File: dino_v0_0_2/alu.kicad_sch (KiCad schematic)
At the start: 0 parts

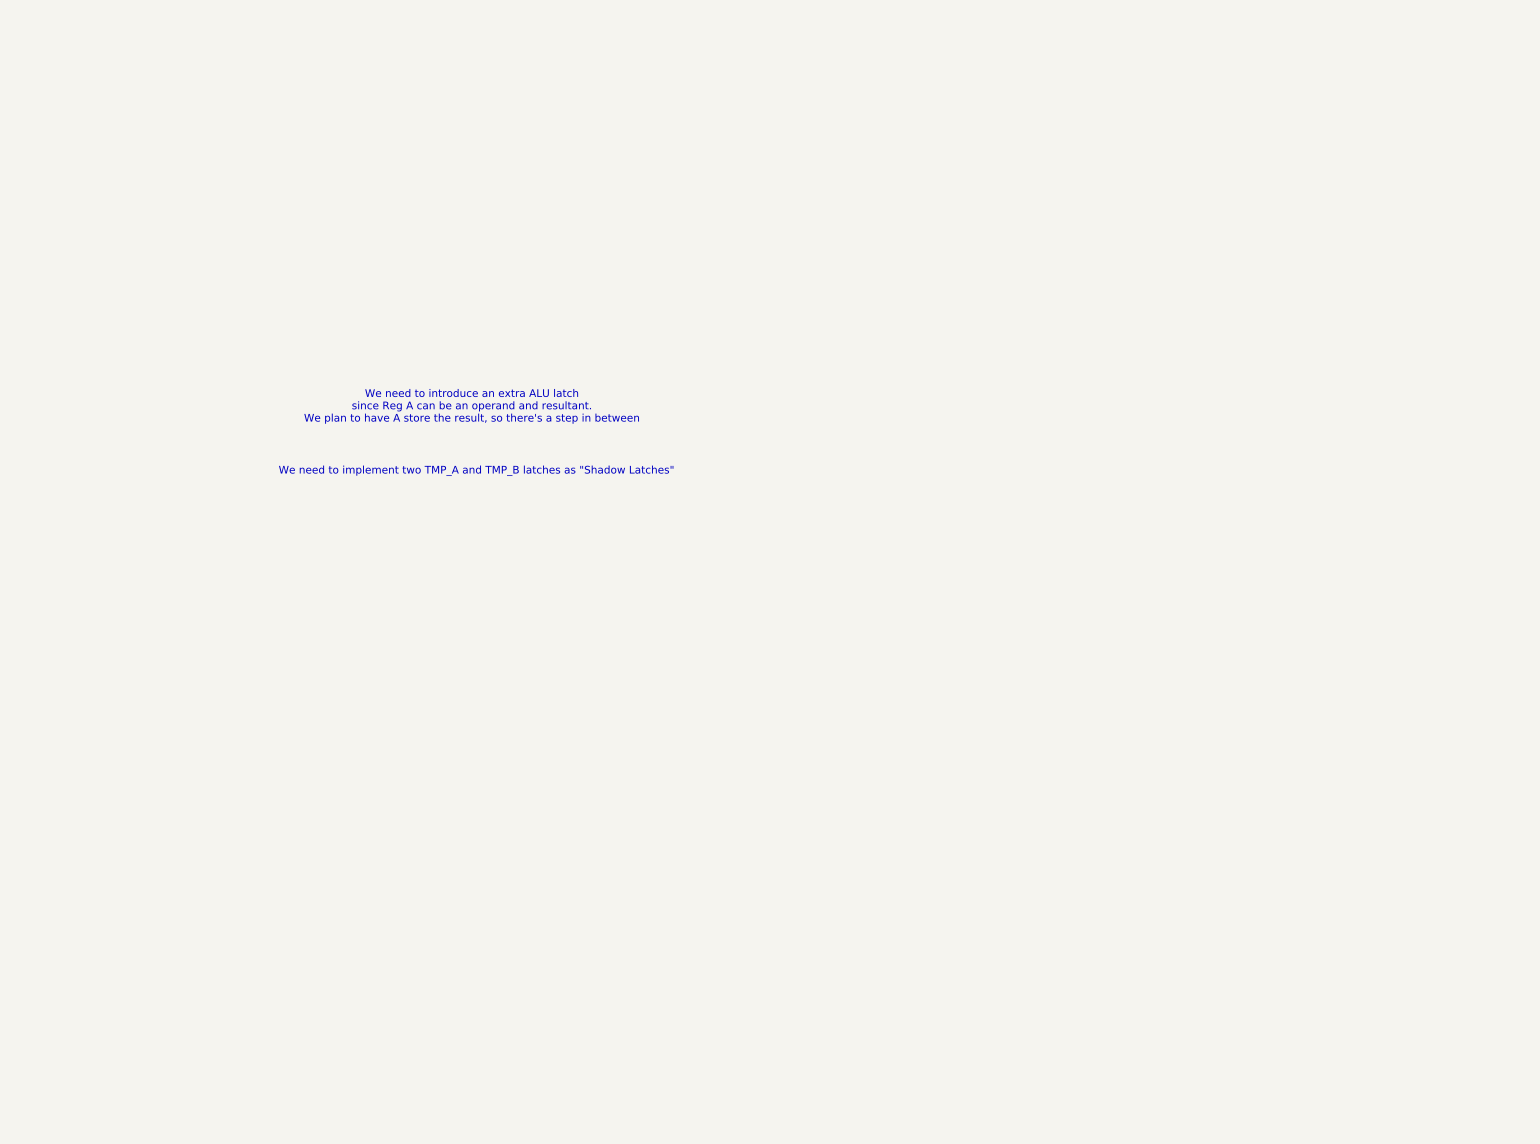
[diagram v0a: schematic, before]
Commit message: DINO v0.0.3: complete ALU/control-word, add MAR+reset sheets, wire reset circuit
ALU sheet: flags register moved from '173 (not in stock) to '273 + a '157
mux to emulate the missing load-enable pins; Z-detect built from a NOR+AND
De Morgan tree instead of a '260; ALU_CIN built from NAND(SA1,SA0) reusing
two already-placed spare gates instead of a dedicated XOR/'86. Sheet is
now fully wired and netlist-clean.

Control word sheet: all 16 CW bits assigned and wired (3x '138 decoders
for the load/source/misc fields, direct bus taps for HALT/PC_MAR_MUX/
PC_UP/END and the ALU SA[2:0] select). Found and fixed several cross-
sheet signal-name mismatches this uncovered (OUT_REG_LOAD/REG_OUT_LOAD,
PC_MAR_MUX/PC_MUX, T-state counter labels, a mirror-reversed IRB->ROM-
address buffer in microcode).

New: MAR and reset sheets, wired into the root hierarchy. Reset circuit
is a from-scratch design: RC+button+74HC14 Schmitt front end feeds the
async PRESET of the clock cluster's spare '74 half (U27B), synchronizing
release to CLK; its Q/~Q fan out to the flags register, the T-state
counter's clear, and (OR'd with the existing microcode-driven PC_CLEAR,
reusing spare gates on the same '02) the PC counters' clear.

Deprecated 7 schematic files no longer referenced by the root sheet's
hierarchy into dino_v0_0_2/deprecated/. Added docs/notes/kicad_netlist.py,
a .kicad_sch connectivity auditor (pin/net resolution incl. buses and
same-name local-label merging) used throughout this session to find the
above bugs; archived completed-work docs into docs/notes/Done/ and
rewrote dino_session_state.md as the current authoritative state+TODO.

Co-Authored-By: Claude Sonnet 5 <noreply@anthropic.com>
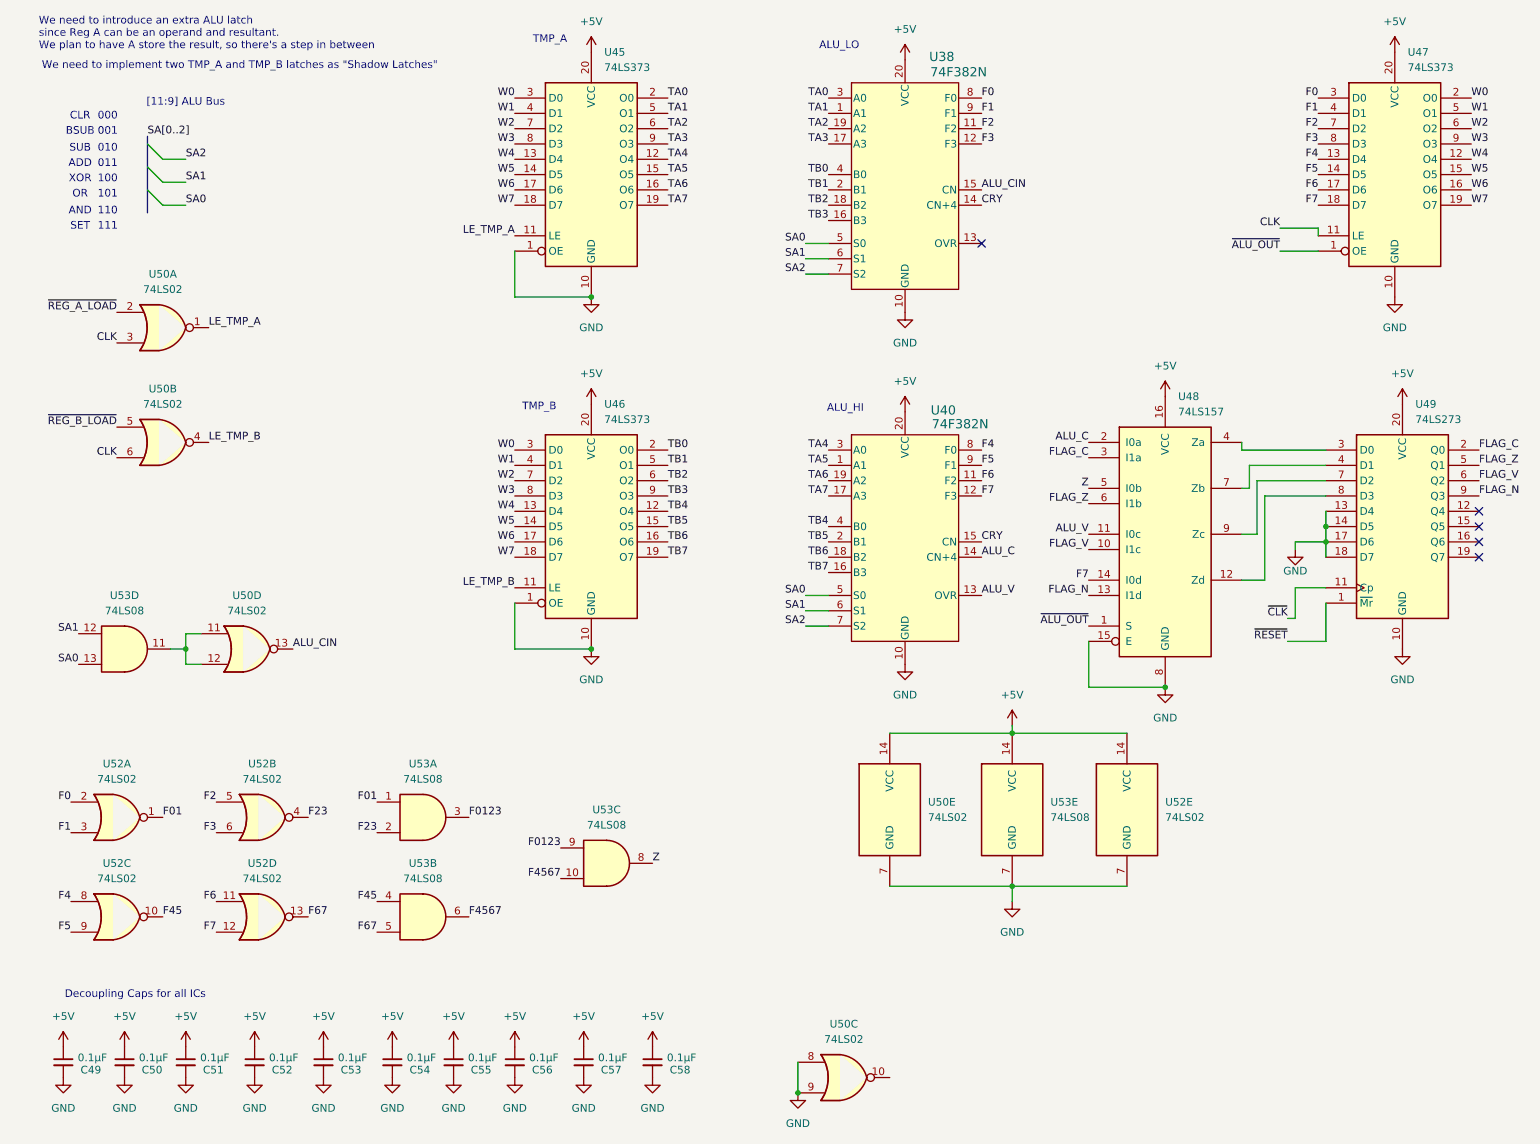
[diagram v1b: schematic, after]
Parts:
- added C49, C50, C51, C52, C53, C54, C55, C56, C57, C58: 0.1µF, symbol Device:C_Small
- added U38, U40: 74F382N, PDIP20_26P42X6P6_ONS, symbol 2026-07-13_03-50-17:74F382PC
- added U45, U46, U47: 74LS373, symbol 74xx:74LS373
- added U48: 74LS157, symbol 74xx:74LS157
- added U49: 74LS273, symbol 74xx:74LS273
- added U50, U52: 74LS02, symbol 74xx:74LS02
- added U53: 74LS08, symbol 74xx:74LS08
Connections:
- new net: U48.4 (Za), U49.3 (D0)
- new net: U48.7 (Zb), U49.4 (D1)
- new net: U48.9 (Zc), U49.7 (D2)
- new net: U48.12 (Zd), U49.8 (D3)
- new net: U50.11, U50.12, U53.11
- new net +5V: C49.1, C50.1, C51.1, C52.1, C53.1, C54.1, C55.1, C56.1, C57.1, C58.1, U38.20 (VCC), U40.20 (VCC), U45.20 (VCC), U46.20 (VCC), U47.20 (VCC), U48.16 (VCC), U49.20 (VCC), U50.14 (VCC), U52.14 (VCC), U53.14 (VCC)
- new net ALU_C: U40.14 (CN+4), U48.2 (I0a)
- new net ALU_CIN: U38.15 (CN), U50.13
- new net ALU_V: U40.13 (OVR), U48.11 (I0c)
- new net CLK: U47.11 (LE), U50.3, U50.6
- new net CRY: U38.14 (CN+4), U40.15 (CN)
- new net F0: U38.8 (F0), U47.3 (D0), U52.2
- new net F01: U52.1, U53.1
- new net F0123: U53.3, U53.9
- new net F1: U38.9 (F1), U47.4 (D1), U52.3
- new net F2: U38.11 (F2), U47.7 (D2), U52.5
- new net F23: U52.4, U53.2
- new net F3: U38.12 (F3), U47.8 (D3), U52.6
- new net F4: U40.8 (F0), U47.13 (D4), U52.8
- new net F45: U52.10, U53.4
- new net F4567: U53.10, U53.6
- new net F5: U40.9 (F1), U47.14 (D5), U52.9
- new net F6: U40.11 (F2), U47.17 (D6), U52.11
- new net F67: U52.13, U53.5
- new net F7: U40.12 (F3), U47.18 (D7), U48.14 (I0d), U52.12
- new net FLAG_C: U48.3 (I1a), U49.2 (Q0)
- new net FLAG_N: U48.13 (I1d), U49.9 (Q3)
- new net FLAG_V: U48.10 (I1c), U49.6 (Q2)
- new net FLAG_Z: U48.6 (I1b), U49.5 (Q1)
- new net GND: C49.2, C50.2, C51.2, C52.2, C53.2, C54.2, C55.2, C56.2, C57.2, C58.2, U38.10 (GND), U40.10 (GND), U45.1 (OE), U45.10 (GND), U46.1 (OE), U46.10 (GND), U47.10 (GND), U48.15 (E), U48.8 (GND), U49.10 (GND), U49.13 (D4), U49.14 (D5), U49.17 (D6), U49.18 (D7), U50.7 (GND), U50.8, U50.9, U52.7 (GND), U53.7 (GND)
- new net LE_TMP_A: U45.11 (LE), U50.1
- new net LE_TMP_B: U46.11 (LE), U50.4
- new net SA0: U38.5 (S0), U40.5 (S0), U53.13
- new net SA1: U38.6 (S1), U40.6 (S1), U53.12
- new net SA2: U38.7 (S2), U40.7 (S2)
- new net TA0: U38.3 (A0), U45.2 (O0)
- new net TA1: U38.1 (A1), U45.5 (O1)
- new net TA2: U38.19 (A2), U45.6 (O2)
- new net TA3: U38.17 (A3), U45.9 (O3)
- new net TA4: U40.3 (A0), U45.12 (O4)
- new net TA5: U40.1 (A1), U45.15 (O5)
- new net TA6: U40.19 (A2), U45.16 (O6)
- new net TA7: U40.17 (A3), U45.19 (O7)
- new net TB0: U38.4 (B0), U46.2 (O0)
- new net TB1: U38.2 (B1), U46.5 (O1)
- new net TB2: U38.18 (B2), U46.6 (O2)
- new net TB3: U38.16 (B3), U46.9 (O3)
- new net TB4: U40.4 (B0), U46.12 (O4)
- new net TB5: U40.2 (B1), U46.15 (O5)
- new net TB6: U40.18 (B2), U46.16 (O6)
- new net TB7: U40.16 (B3), U46.19 (O7)
- new net W0: U45.3 (D0), U46.3 (D0), U47.2 (O0)
- new net W1: U45.4 (D1), U46.4 (D1), U47.5 (O1)
- new net W2: U45.7 (D2), U46.7 (D2), U47.6 (O2)
- new net W3: U45.8 (D3), U46.8 (D3), U47.9 (O3)
- new net W4: U45.13 (D4), U46.13 (D4), U47.12 (O4)
- new net W5: U45.14 (D5), U46.14 (D5), U47.15 (O5)
- new net W6: U45.17 (D6), U46.17 (D6), U47.16 (O6)
- new net W7: U45.18 (D7), U46.18 (D7), U47.19 (O7)
- new net Z: U48.5 (I0b), U53.8
- new net ~{ALU_OUT}: U47.1 (OE), U48.1 (S)
- new net ~{CLK}: U49.11 (Cp)
- new net ~{REG_A_LOAD}: U50.2
- new net ~{REG_B_LOAD}: U50.5
- new net ~{RESET}: U49.1 (~{Mr})
- no-connect marks 0 -> 5
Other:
- note added: "000"
- note added: "001"
- note added: "010"
- note added: "011"
- note added: "100"
- note added: "101"
- note added: "110"
- note added: "111"
- note added: "ADD"
- note added: "ALU_HI"
- note added: "ALU_LO"
- note added: "AND"
- note added: "BSUB"
- note added: "CLR"
- note added: "Decoupling Caps for all ICs"
- note added: "OR"
- note added: "SET"
- note added: "SUB"
- note added: "TMP_A"
- note added: "TMP_B"
- note added: "XOR"
- note added: "[11:9] ALU Bus"
